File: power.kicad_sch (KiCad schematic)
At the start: 0 parts

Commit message: changed mcu and added power
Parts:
- added C19, C20: 10u, Capacitor_SMD:C_0805_2012Metric, symbol Device:C
- added J4: USB_B_Micro, Connector_USB:USB_Micro-B_Amphenol_10103594-0001LF_Horizontal, symbol Connector:USB_B_Micro
- added U11: NCP1117-3.3_SOT223, Package_TO_SOT_SMD:SOT-223-3_TabPin2, symbol Regulator_Linear:NCP1117-3.3_SOT223
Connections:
- new net +3.3V: C20.1, U11.2 (VO)
- new net +5V: C19.1, J4.1 (VBUS), U11.3 (VI)
- new net GND: C19.2, C20.2, J4.5 (GND), J4.6 (Shield), U11.1 (GND)
- no-connect marks 0 -> 3
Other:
- note added: "Power"

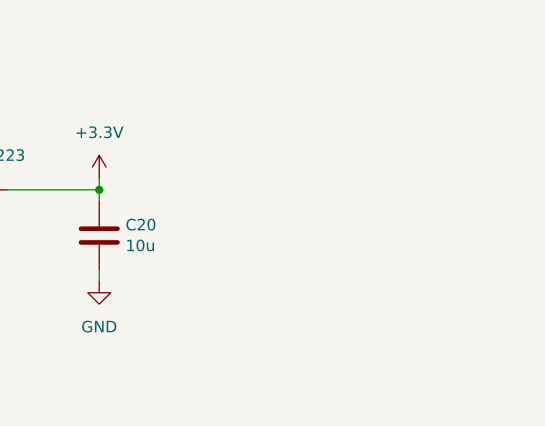
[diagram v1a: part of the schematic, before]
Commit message: added MCU decaps and hall effect schematic
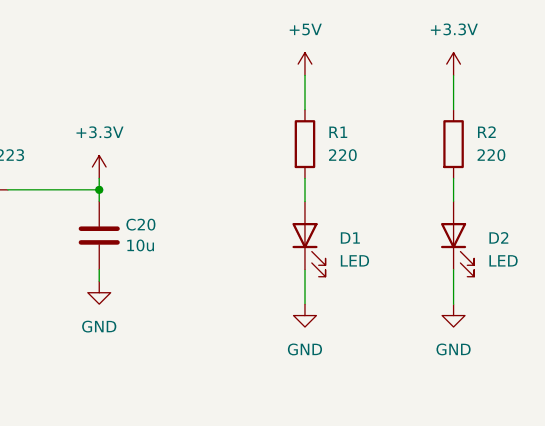
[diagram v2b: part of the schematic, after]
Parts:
- added D1, D2: LED, symbol Device:LED
- added R1, R2: 220, symbol Device:R
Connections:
- net +3.3V: now also R2.1
- net +5V: now also R1.1
- net GND: now also D1.1 (K), D2.1 (K)
- new net: D2.2 (A), R2.2
- new net: D1.2 (A), R1.2

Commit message: layout
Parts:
- D1, D2: footprint (none) -> LED_SMD:LED_0805_2012Metric
- R1, R2: footprint (none) -> Resistor_SMD:R_0805_2012Metric
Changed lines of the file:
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@@
 			)
 		)
-		(property "Footprint" ""
+		(property "Footprint" "Resistor_SMD:R_0805_2012Metric"
 			(at 198.882 67.31 90)
 			(effects
@@
 			)
 		)
-		(property "Footprint" ""
+		(property "Footprint" "Resistor_SMD:R_0805_2012Metric"
 			(at 182.372 67.31 90)
 			(effects
@@
 			)
 		)
-		(property "Footprint" ""
+		(property "Footprint" "LED_SMD:LED_0805_2012Metric"
 			(at 184.15 77.47 0)
 			(effects
@@
 			)
 		)
-		(property "Footprint" ""
+		(property "Footprint" "LED_SMD:LED_0805_2012Metric"
 			(at 200.66 77.47 0)
 			(effects

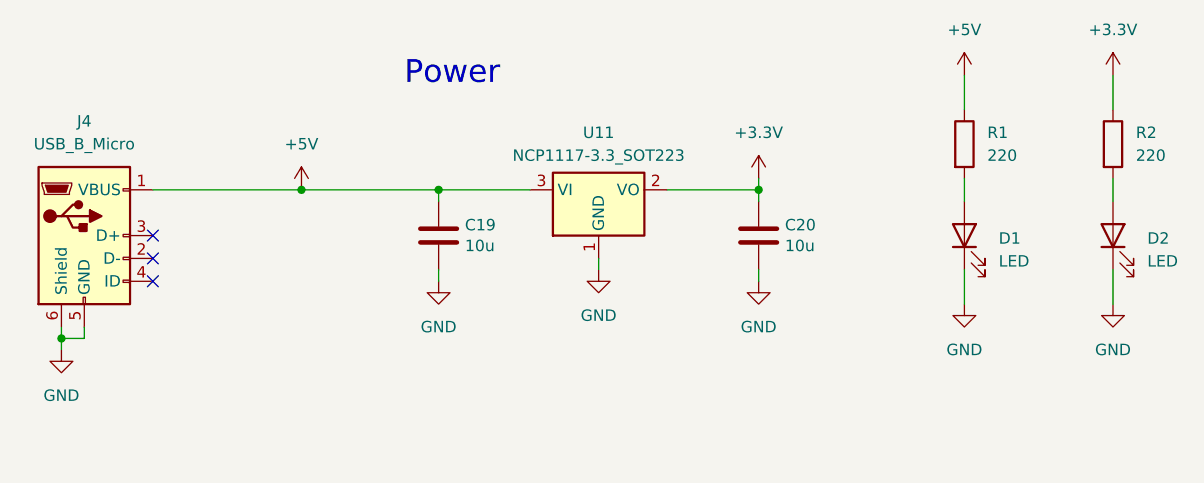
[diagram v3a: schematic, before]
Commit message: cleaned up MCU and added some debugging circuitry
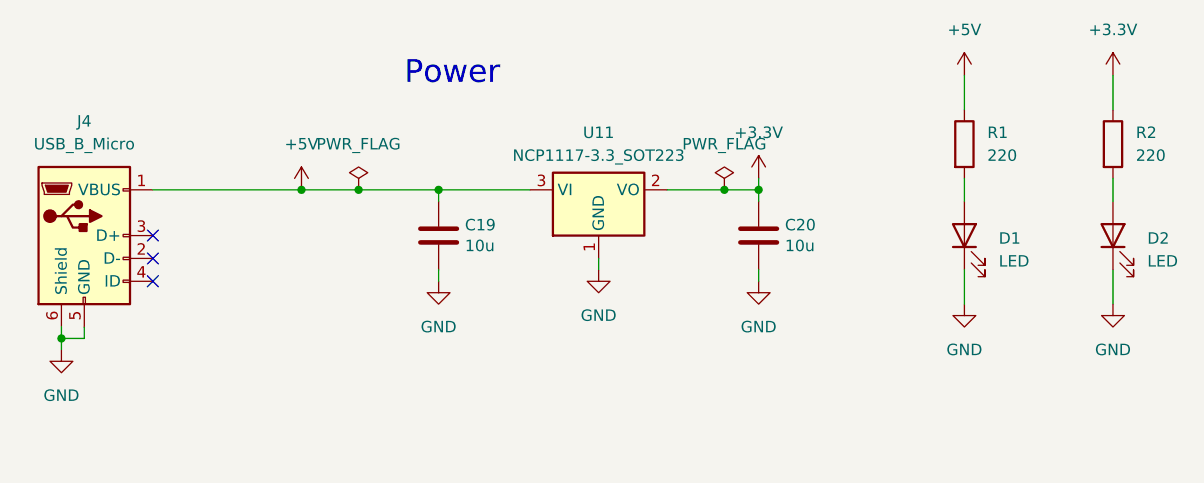
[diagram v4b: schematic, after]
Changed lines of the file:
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@@
+	)
+	(junction
+		(at 116.84 72.39)
+		(diameter 0)
+		(color 0 0 0 0)
 	)
 	(junction
@@
 		(color 0 0 0 0)
 	)
+	(junction
+		(at 157.48 72.39)
+		(diameter 0)
+		(color 0 0 0 0)
+	)
 	(no_connect
 		(at 93.98 77.47)
@@
 	(wire
 		(pts
-			(xy 110.49 72.39) (xy 125.73 72.39)
+			(xy 110.49 72.39) (xy 116.84 72.39)
 		)
 		(stroke
@@
 	(wire
 		(pts
+			(xy 157.48 72.39) (xy 161.29 72.39)
+		)
+		(stroke
+			(width 0)
+			(type default)
+		)
+	)
+	(wire
+		(pts
 			(xy 184.15 71.12) (xy 184.15 73.66)
 		)
@@
 	(wire
 		(pts
+			(xy 116.84 72.39) (xy 125.73 72.39)
+		)
+		(stroke
+			(width 0)
+			(type default)
+		)
+	)
+	(wire
+		(pts
 			(xy 125.73 73.66) (xy 125.73 72.39)
 		)
@@
 	(wire
 		(pts
-			(xy 151.13 72.39) (xy 161.29 72.39)
+			(xy 151.13 72.39) (xy 157.48 72.39)
 		)
 		(stroke
@@
 					(unit 1)
 				)
+			)
+		)
+	)
+	(symbol
+		(lib_id "power:PWR_FLAG")
+		(at 157.48 72.39 0)
+		(unit 1)
+		(exclude_from_sim no)
+		(in_bom yes)
+		(on_board yes)
+		(dnp no)
+		(fields_autoplaced yes)
+		(property "Reference" "#FLG02"
+			(at 157.48 70.485 0)
+			(effects
+				(font
+					(size 1.27 1.27)
+				)
+				(hide yes)
+			)
+		)
+		(property "Value" "PWR_FLAG"
+			(at 157.48 67.31 0)
+			(effects
+				(font
+					(size 1.27 1.27)
+				)
+			)
+		)
+		(property "Footprint" ""
+			(at 157.48 72.39 0)
+			(effects
+				(font
+					(size 1.27 1.27)
+				)
+				(hide yes)
+			)
+		)
+		(property "Datasheet" "~"
+			(at 157.48 72.39 0)
+			(effects
+				(font
+					(size 1.27 1.27)
+				)
+				(hide yes)
+			)
+		)
+		(property "Description" "Special symbol for telling ERC where power comes from"
+			(at 157.48 72.39 0)
+			(effects
+				(font
+					(size 1.27 1.27)
+				)
+				(hide yes)
+			)
+		)
+		(pin "1"
+		)
+		(instances
+			(project "senior_design"
+				(path "/35c074f0-8545-4dc1-a57d-3ef0bc7d9188/6a3bd25b-0e65-4984-bc83-1e0aa4753ca0"
+					(reference "#FLG02")
+					(unit 1)
+				)
+			)
+		)
+	)
+	(symbol
+		(lib_id "power:PWR_FLAG")
+		(at 116.84 72.39 0)
+		(unit 1)
+		(exclude_from_sim no)
+		(in_bom yes)
+		(on_board yes)
+		(dnp no)
+		(fields_autoplaced yes)
+		(property "Reference" "#FLG01"
+			(at 116.84 70.485 0)
+			(effects
+				(font
+					(size 1.27 1.27)
+				)
+				(hide yes)
+			)
+		)
+		(property "Value" "PWR_FLAG"
+			(at 116.84 67.31 0)
+			(effects
+				(font
+					(size 1.27 1.27)
+				)
+			)
+		)
+		(property "Footprint" ""
+			(at 116.84 72.39 0)
+			(effects
+				(font
+					(size 1.27 1.27)
+				)
+				(hide yes)
+			)
+		)
+		(property "Datasheet" "~"
+			(at 116.84 72.39 0)
+			(effects
+				(font
+					(size 1.27 1.27)
+				)
+				(hide yes)
+			)
+		)
+		(property "Description" "Special symbol for telling ERC where power comes from"
+			(at 116.84 72.39 0)
+			(effects
+				(font
+					(size 1.27 1.27)
+				)
+				(hide yes)
+			)
+		)
+		(pin "1"
+		)
+		(instances
+			(project ""
+				(path "/35c074f0-8545-4dc1-a57d-3ef0bc7d9188/6a3bd25b-0e65-4984-bc83-1e0aa4753ca0"
+					(reference "#FLG01")
+					(unit 1)
+				)

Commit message: Added names on silkscreen and mounting holes
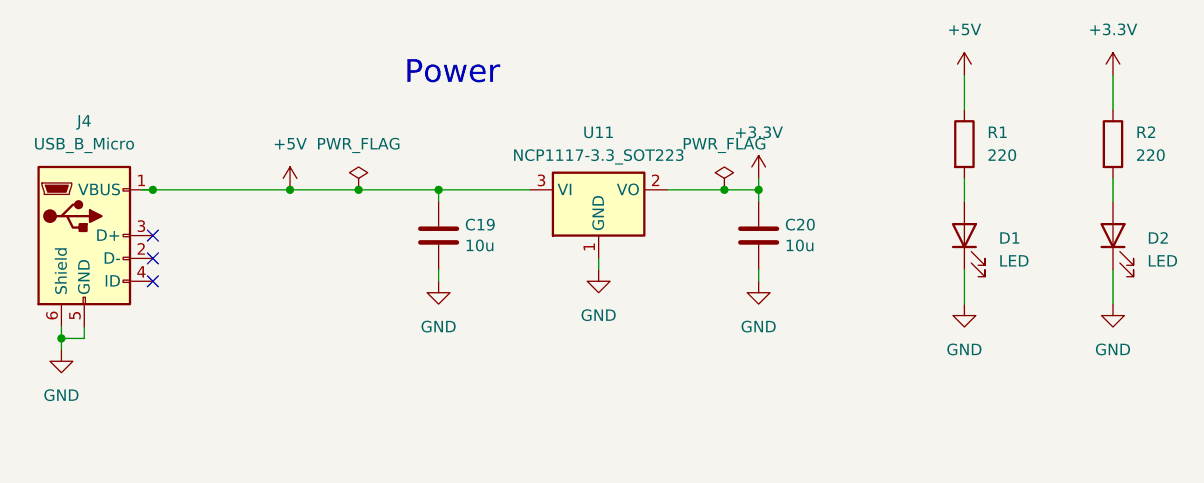
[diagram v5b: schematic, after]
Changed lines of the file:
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@@
 	)
 	(junction
-		(at 110.49 72.39)
+		(at 93.98 72.39)
+		(diameter 0)
+		(color 0 0 0 0)
+	)
+	(junction
+		(at 109.22 72.39)
 		(diameter 0)
 		(color 0 0 0 0)
@@
 	(wire
 		(pts
-			(xy 110.49 72.39) (xy 116.84 72.39)
+			(xy 93.98 72.39) (xy 109.22 72.39)
+		)
+		(stroke
+			(width 0)
+			(type default)
+		)
+	)
+	(wire
+		(pts
+			(xy 109.22 72.39) (xy 116.84 72.39)
 		)
 		(stroke
@@
 	(wire
 		(pts
-			(xy 93.98 72.39) (xy 110.49 72.39)
+			(xy 92.71 72.39) (xy 93.98 72.39)
 		)
 		(stroke
@@
 	(symbol
 		(lib_id "power:VCC")
-		(at 110.49 72.39 0)
+		(at 109.22 72.39 0)
 		(unit 1)
 		(exclude_from_sim no)
@@
 		(fields_autoplaced yes)
 		(property "Reference" "#PWR037"
-			(at 110.49 76.2 0)
+			(at 109.22 76.2 0)
 			(effects
 				(font
@@
 		)
 		(property "Value" "+5V"
-			(at 110.49 67.31 0)
+			(at 109.22 67.31 0)
 			(effects
 				(font
@@
 		)
 		(property "Footprint" ""
-			(at 110.49 72.39 0)
+			(at 109.22 72.39 0)
 			(effects
 				(font
@@
 		)
 		(property "Datasheet" ""
-			(at 110.49 72.39 0)
+			(at 109.22 72.39 0)
 			(effects
 				(font
@@
 		)
 		(property "Description" "Power symbol creates a global label with name \"VCC\""
-			(at 110.49 72.39 0)
-			(effects
-				(font
+			(at 109.22 72.39 0)
+			(effects
+				(font

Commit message: Updated Schematic
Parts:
- added D5: PTVS5V0Z1USK, Diode_SMD:Nexperia_DSN1608-2_1.6x0.8mm, symbol Diode:PTVS5V0Z1USK
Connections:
- net +5V: now also D5.1 (K)
- net GND: now also D5.2 (A)
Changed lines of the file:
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@@
+	)
+	(junction
+		(at 99.06 72.39)
+		(diameter 0)
+		(color 0 0 0 0)
 	)
 	(junction
@@
 	(wire
 		(pts
+			(xy 99.06 72.39) (xy 109.22 72.39)
+		)
+		(stroke
+			(width 0)
+			(type default)
+		)
+	)
+	(wire
+		(pts
 			(xy 83.82 88.9) (xy 83.82 90.17)
 		)
@@
 	(wire
 		(pts
-			(xy 93.98 72.39) (xy 109.22 72.39)
+			(xy 93.98 72.39) (xy 99.06 72.39)
 		)
 		(stroke
@@
 	)
 	(symbol
+		(lib_id "Diode:PTVS5V0Z1USK")
+		(at 99.06 76.2 270)
+		(unit 1)
+		(exclude_from_sim no)
+		(in_bom yes)
+		(on_board yes)
+		(dnp no)
+		(fields_autoplaced yes)
+		(property "Reference" "D5"
+			(at 101.6 74.9299 90)
+			(effects
+				(font
+					(size 1.27 1.27)
+				)
+				(justify left)
+			)
+		)
+		(property "Value" "PTVS5V0Z1USK"
+			(at 101.6 77.4699 90)
+			(effects
+				(font
+					(size 1.27 1.27)
+				)
+				(justify left)
+			)
+		)
+		(property "Footprint" "Diode_SMD:Nexperia_DSN1608-2_1.6x0.8mm"
+			(at 94.615 76.2 0)
+			(effects
+				(font
+					(size 1.27 1.27)
+				)
+				(hide yes)
+			)
+		)
+		(property "Datasheet" "https://assets.nexperia.com/documents/data-sheet/PTVS5V0Z1USK.pdf"
+			(at 99.06 76.2 0)
+			(effects
+				(font
+					(size 1.27 1.27)
+				)
+				(hide yes)
+			)
+		)
+		(property "Description" "5V, 1200W TVS unidirectional diode, DSN1608-2"
+			(at 99.06 76.2 0)
+			(effects
+				(font
+					(size 1.27 1.27)
+				)
+				(hide yes)
+			)
+		)
+		(pin "1"
+		)
+		(pin "2"
+		)
+		(instances
+			(project ""
+				(path "/35c074f0-8545-4dc1-a57d-3ef0bc7d9188/6a3bd25b-0e65-4984-bc83-1e0aa4753ca0"
+					(reference "D5")
+					(unit 1)
+				)
+			)
+		)
+	)
+	(symbol
 		(lib_id "Device:R")
 		(at 200.66 67.31 0)
@@
 					(unit 1)
 				)
+			)
+		)
+	)
+	(symbol
+		(lib_id "power:GND")
+		(at 99.06 80.01 0)
+		(unit 1)
+		(exclude_from_sim no)
+		(in_bom yes)
+		(on_board yes)
+		(dnp no)
+		(fields_autoplaced yes)
+		(property "Reference" "#PWR070"
+			(at 99.06 86.36 0)
+			(effects
+				(font
+					(size 1.27 1.27)
+				)
+				(hide yes)
+			)
+		)
+		(property "Value" "GND"
+			(at 99.06 85.09 0)
+			(effects
+				(font
+					(size 1.27 1.27)
+				)
+			)
+		)
+		(property "Footprint" ""
+			(at 99.06 80.01 0)
+			(effects
+				(font
+					(size 1.27 1.27)
+				)
+				(hide yes)
+			)
+		)
+		(property "Datasheet" ""
+			(at 99.06 80.01 0)
+			(effects
+				(font
+					(size 1.27 1.27)
+				)
+				(hide yes)
+			)
+		)
+		(property "Description" "Power symbol creates a global label with name \"GND\" , ground"
+			(at 99.06 80.01 0)
+			(effects
+				(font
+					(size 1.27 1.27)
+				)
+				(hide yes)
+			)
+		)
+		(pin "1"
+		)
+		(instances
+			(project ""
+				(path "/35c074f0-8545-4dc1-a57d-3ef0bc7d9188/6a3bd25b-0e65-4984-bc83-1e0aa4753ca0"
+					(reference "#PWR070")
+					(unit 1)
+				)

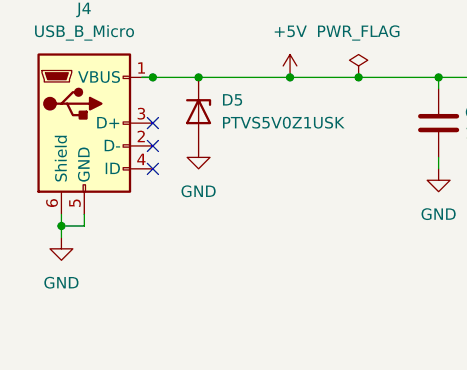
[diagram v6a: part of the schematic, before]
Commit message: Fixed labels and added datasheets
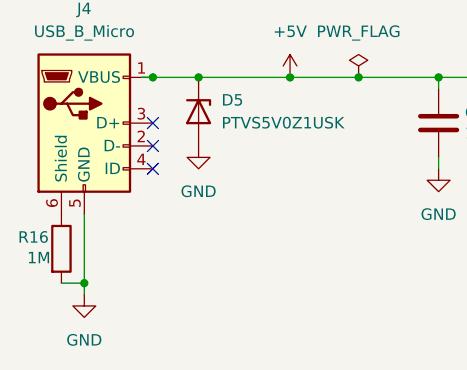
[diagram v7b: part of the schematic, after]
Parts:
- added R16: 1M, Resistor_SMD:R_0805_2012Metric, symbol Device:R
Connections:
- net GND: now also R16.2; no longer J4.6 (Shield)
- new net: J4.6 (Shield), R16.1
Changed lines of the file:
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@@
 	)
 	(junction
-		(at 83.82 88.9)
+		(at 86.36 95.25)
 		(diameter 0)
 		(color 0 0 0 0)
@@
 	(wire
 		(pts
-			(xy 86.36 88.9) (xy 83.82 88.9)
-		)
-		(stroke
-			(width 0)
-			(type default)
-		)
-	)
-	(wire
-		(pts
 			(xy 99.06 72.39) (xy 109.22 72.39)
 		)
@@
 	(wire
 		(pts
-			(xy 83.82 88.9) (xy 83.82 90.17)
+			(xy 86.36 87.63) (xy 86.36 95.25)
+		)
+		(stroke
+			(width 0)
+			(type default)
+		)
+	)
+	(wire
+		(pts
+			(xy 86.36 95.25) (xy 86.36 96.52)
 		)
 		(stroke
@@
 	(wire
 		(pts
-			(xy 83.82 87.63) (xy 83.82 88.9)
-		)
-		(stroke
-			(width 0)
-			(type default)
-		)
-	)
-	(wire
-		(pts
 			(xy 92.71 72.39) (xy 93.98 72.39)
 		)
@@
 	(wire
 		(pts
+			(xy 83.82 95.25) (xy 86.36 95.25)
+		)
+		(stroke
+			(width 0)
+			(type default)
+		)
+	)
+	(wire
+		(pts
 			(xy 157.48 72.39) (xy 161.29 72.39)
 		)
@@
 		(pts
 			(xy 184.15 81.28) (xy 184.15 85.09)
-		)
-		(stroke
-			(width 0)
-			(type default)
-		)
-	)
-	(wire
-		(pts
-			(xy 86.36 87.63) (xy 86.36 88.9)
 		)
 		(stroke
@@
 	)
 	(symbol
+		(lib_id "Device:R")
+		(at 83.82 91.44 0)
+		(unit 1)
+		(exclude_from_sim no)
+		(in_bom yes)
+		(on_board yes)
+		(dnp no)
+		(property "Reference" "R16"
+			(at 78.994 90.17 0)
+			(effects
+				(font
+					(size 1.27 1.27)
+				)
+				(justify left)
+			)
+		)
+		(property "Value" "1M"
+			(at 80.01 92.456 0)
+			(effects
+				(font
+					(size 1.27 1.27)
+				)
+				(justify left)
+			)
+		)
+		(property "Footprint" "Resistor_SMD:R_0805_2012Metric"
+			(at 82.042 91.44 90)
+			(effects
+				(font
+					(size 1.27 1.27)
+				)
+				(hide yes)
+			)
+		)
+		(property "Datasheet" "~"
+			(at 83.82 91.44 0)
+			(effects
+				(font
+					(size 1.27 1.27)
+				)
+				(hide yes)
+			)
+		)
+		(property "Description" "Resistor"
+			(at 83.82 91.44 0)
+			(effects
+				(font
+					(size 1.27 1.27)
+				)
+				(hide yes)
+			)
+		)
+		(pin "1"
+		)
+		(pin "2"
+		)
+		(instances
+			(project ""
+				(path "/35c074f0-8545-4dc1-a57d-3ef0bc7d9188/6a3bd25b-0e65-4984-bc83-1e0aa4753ca0"
+					(reference "R16")
+					(unit 1)
+				)
+			)
+		)
+	)
+	(symbol
 		(lib_id "power:PWR_FLAG")
 		(at 116.84 72.39 0)
@@
 		(lib_name "GND_1")
 		(lib_id "power:GND")
-		(at 83.82 90.17 0)
+		(at 86.36 96.52 0)
 		(unit 1)
 		(exclude_from_sim no)
@@
 		(fields_autoplaced yes)
 		(property "Reference" "#PWR065"
-			(at 83.82 96.52 0)
+			(at 86.36 102.87 0)
 			(effects
 				(font
@@
 		)
 		(property "Value" "GND"
-			(at 83.82 95.25 0)
+			(at 86.36 101.6 0)
 			(effects
 				(font
@@
 		)
 		(property "Footprint" ""
-			(at 83.82 90.17 0)
+			(at 86.36 96.52 0)
 			(effects
 				(font
@@
 		)
 		(property "Datasheet" ""
-			(at 83.82 90.17 0)
+			(at 86.36 96.52 0)
 			(effects
 				(font
@@
 		)
 		(property "Description" "Power symbol creates a global label with name \"GND\" , ground"
-			(at 83.82 90.17 0)
-			(effects
-				(font
+			(at 86.36 96.52 0)
+			(effects
+				(font

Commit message: Feedback Final Update
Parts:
- added D13: D_Schottky, SS14 Schottky:DIONM4336X250N, symbol Device:D_Schottky
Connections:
- net +5V: now also D13.1 (K); no longer D5.1 (K), J4.1 (VBUS)
- new net: D13.2 (A), D5.1 (K), J4.1 (VBUS)
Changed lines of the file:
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@@
+	)
+	(junction
+		(at 99.06 72.39)
+		(diameter 0)
+		(color 0 0 0 0)
+	)
+	(junction
+		(at 116.84 72.39)
+		(diameter 0)
+		(color 0 0 0 0)
 	)
 	(junction
 		(at 109.22 72.39)
-		(diameter 0)
-		(color 0 0 0 0)
-	)
-	(junction
-		(at 99.06 72.39)
-		(diameter 0)
-		(color 0 0 0 0)
-	)
-	(junction
-		(at 116.84 72.39)
 		(diameter 0)
 		(color 0 0 0 0)
@@
 	(wire
 		(pts
-			(xy 99.06 72.39) (xy 109.22 72.39)
-		)
-		(stroke
-			(width 0)
-			(type default)
-		)
-	)
-	(wire
-		(pts
 			(xy 86.36 87.63) (xy 86.36 95.25)
 		)
@@
 	(wire
 		(pts
+			(xy 106.68 72.39) (xy 109.22 72.39)
+		)
+		(stroke
+			(width 0)
+			(type default)
+		)
+	)
+	(wire
+		(pts
 			(xy 161.29 81.28) (xy 161.29 82.55)
 		)
@@
 	(wire
 		(pts
+			(xy 92.71 72.39) (xy 93.98 72.39)
+		)
+		(stroke
+			(width 0)
+			(type default)
+		)
+	)
+	(wire
+		(pts
+			(xy 83.82 95.25) (xy 86.36 95.25)
+		)
+		(stroke
+			(width 0)
+			(type default)
+		)
+	)
+	(wire
+		(pts
+			(xy 157.48 72.39) (xy 161.29 72.39)
+		)
+		(stroke
+			(width 0)
+			(type default)
+		)
+	)
+	(wire
+		(pts
 			(xy 109.22 72.39) (xy 116.84 72.39)
 		)
@@
 	(wire
 		(pts
-			(xy 92.71 72.39) (xy 93.98 72.39)
-		)
-		(stroke
-			(width 0)
-			(type default)
-		)
-	)
-	(wire
-		(pts
-			(xy 83.82 95.25) (xy 86.36 95.25)
-		)
-		(stroke
-			(width 0)
-			(type default)
-		)
-	)
-	(wire
-		(pts
-			(xy 157.48 72.39) (xy 161.29 72.39)
-		)
-		(stroke
-			(width 0)
-			(type default)
-		)
-	)
-	(wire
-		(pts
 			(xy 184.15 71.12) (xy 184.15 73.66)
 		)
@@
 		)
 	)
+	(symbol
+		(lib_id "Device:D_Schottky")
+		(at 102.87 72.39 180)
+		(unit 1)
+		(exclude_from_sim no)
+		(in_bom yes)
+		(on_board yes)
+		(dnp no)
+		(fields_autoplaced yes)
+		(property "Reference" "D13"
+			(at 103.1875 66.04 0)
+			(effects
+				(font
+					(size 1.27 1.27)
+				)
+			)
+		)
+		(property "Value" "D_Schottky"
+			(at 103.1875 68.58 0)
+			(effects
+				(font
+					(size 1.27 1.27)
+				)
+			)
+		)
+		(property "Footprint" "SS14 Schottky:DIONM4336X250N"
+			(at 102.87 72.39 0)
+			(effects
+				(font
+					(size 1.27 1.27)
+				)
+				(hide yes)
+			)
+		)
+		(property "Datasheet" "~"
+			(at 102.87 72.39 0)
+			(effects
+				(font
+					(size 1.27 1.27)
+				)
+				(hide yes)
+			)
+		)
+		(property "Description" "Schottky diode"
+			(at 102.87 72.39 0)
+			(effects
+				(font
+					(size 1.27 1.27)
+				)
+				(hide yes)
+			)
+		)
+		(pin "1"
+		)
+		(pin "2"
+		)
+		(instances
+			(project ""
+				(path "/35c074f0-8545-4dc1-a57d-3ef0bc7d9188/6a3bd25b-0e65-4984-bc83-1e0aa4753ca0"
+					(reference "D13")
+					(unit 1)
+				)
+			)
+		)
+	)
